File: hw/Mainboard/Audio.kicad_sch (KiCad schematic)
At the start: 11 parts, among them J22 AUDIO, U20 LM386

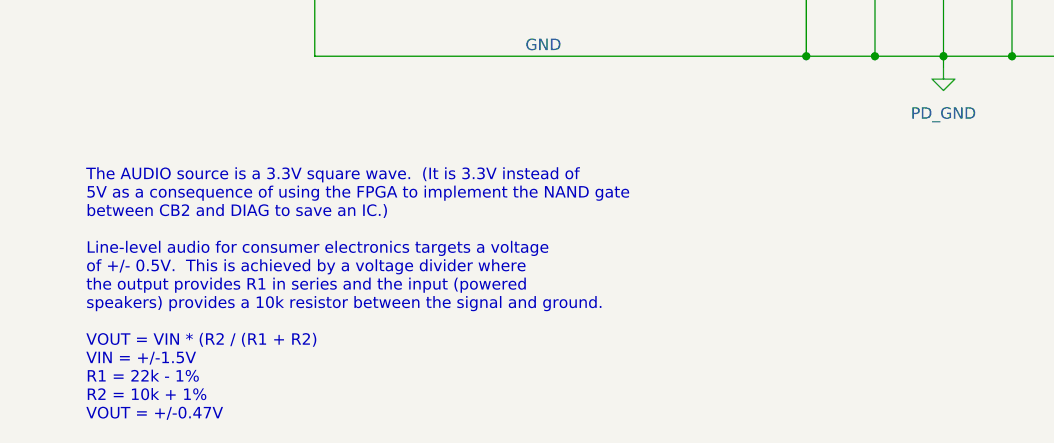
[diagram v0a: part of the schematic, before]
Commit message: docs(hw): describe delta-sigma DAC in schematic
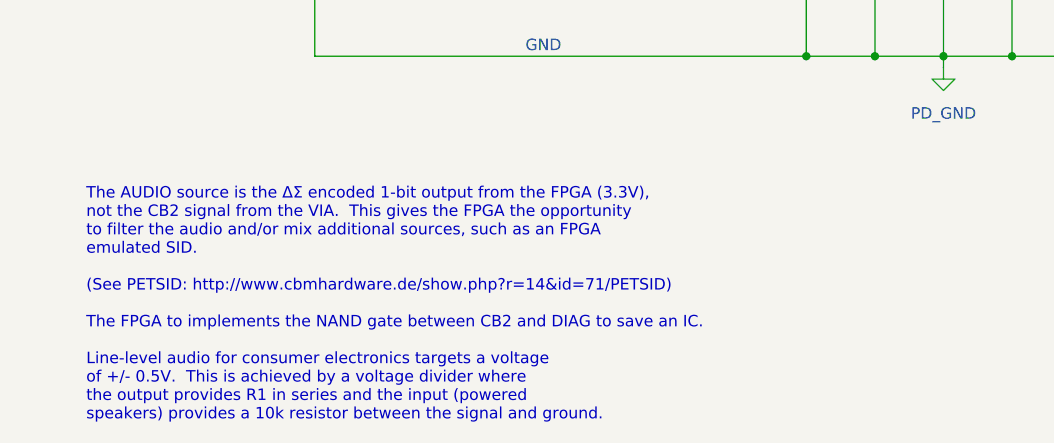
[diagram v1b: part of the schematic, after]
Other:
- note added: "The AUDIO source is the ΔΣ encoded 1-bit output from the FPGA (3.3V), not the CB2 signal from the VIA. This gives the FPGA the opportunity to filter the audio and/or mix additional sources, such as an FPGA emulated SID. (See PETSID: http://www.cbmhardware.de/show.php?r=14&id=71/PETSID) The FPGA to implements the NAND gate between CB2 and DIAG to save an IC. Line-level audio for consumer electroni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"
- note removed: "The AUDIO source is a 3.3V square wave. (It is 3.3V instead of 5V as a consequence of using the FPGA to implement the NAND gate between CB2 and DIAG to save an IC.) Line-level audio for consumer electronics targets a voltage of +/- 0.5V. This is achieved by a voltage divider where the output provides R1 in series and the input (powered speakers) provides a 10k resistor between the signal and grou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"
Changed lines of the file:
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@@
     (stroke (width 0) (type default) (color 0 0 0 0))
   )
-  (text "The AUDIO source is a 3.3V square wave.  (It is 3.3V instead of\n5V as a consequence of using the FPGA to implement the NAND gate\nbetween CB2 and DIAG to save an IC.)\n\nLine-level audio for consumer electronics targets a voltage\nof +/- 0.5V.  This is achieved by a voltage divider where\nthe output provides R1 in series and the input (powered\nspeakers) provides a 10k resistor between the signal and ground.\n\nVOUT = VIN * (R2 / (R1 + R2)\nVIN = +/-1.5V\nR1 = 22k - 1%\nR2 = 10k + 1%\nVOUT = +/-0.47V"
+  (text "The AUDIO source is the ΔΣ encoded 1-bit output from the FPGA (3.3V),\nnot the CB2 signal from the VIA.  This gives the FPGA the opportunity\nto filter the audio and/or mix additional sources, such as an FPGA\nemulated SID.\n\n(See PETSID: http://www.cbmhardware.de/show.php?r=14&id=71/PETSID)\n\nThe FPGA to implements the NAND gate between CB2 and DIAG to save an IC.\n\nLine-level audio for consumer electronics targets a voltage\nof +/- 0.5V.  This is achieved by a voltage divider where\nthe output provides R1 in series and the input (powered\nspeakers) provides a 10k resistor between the signal and ground."
     (at 62.23 139.7 0)
     (effects (font (size 1.27 1.27)) (justify left bottom))
